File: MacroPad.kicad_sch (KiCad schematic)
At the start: 41 parts, among them J1 USB_C_Receptacle, SW1 SW_Push, U1 ATmega32U4-A, Y1 16MHz

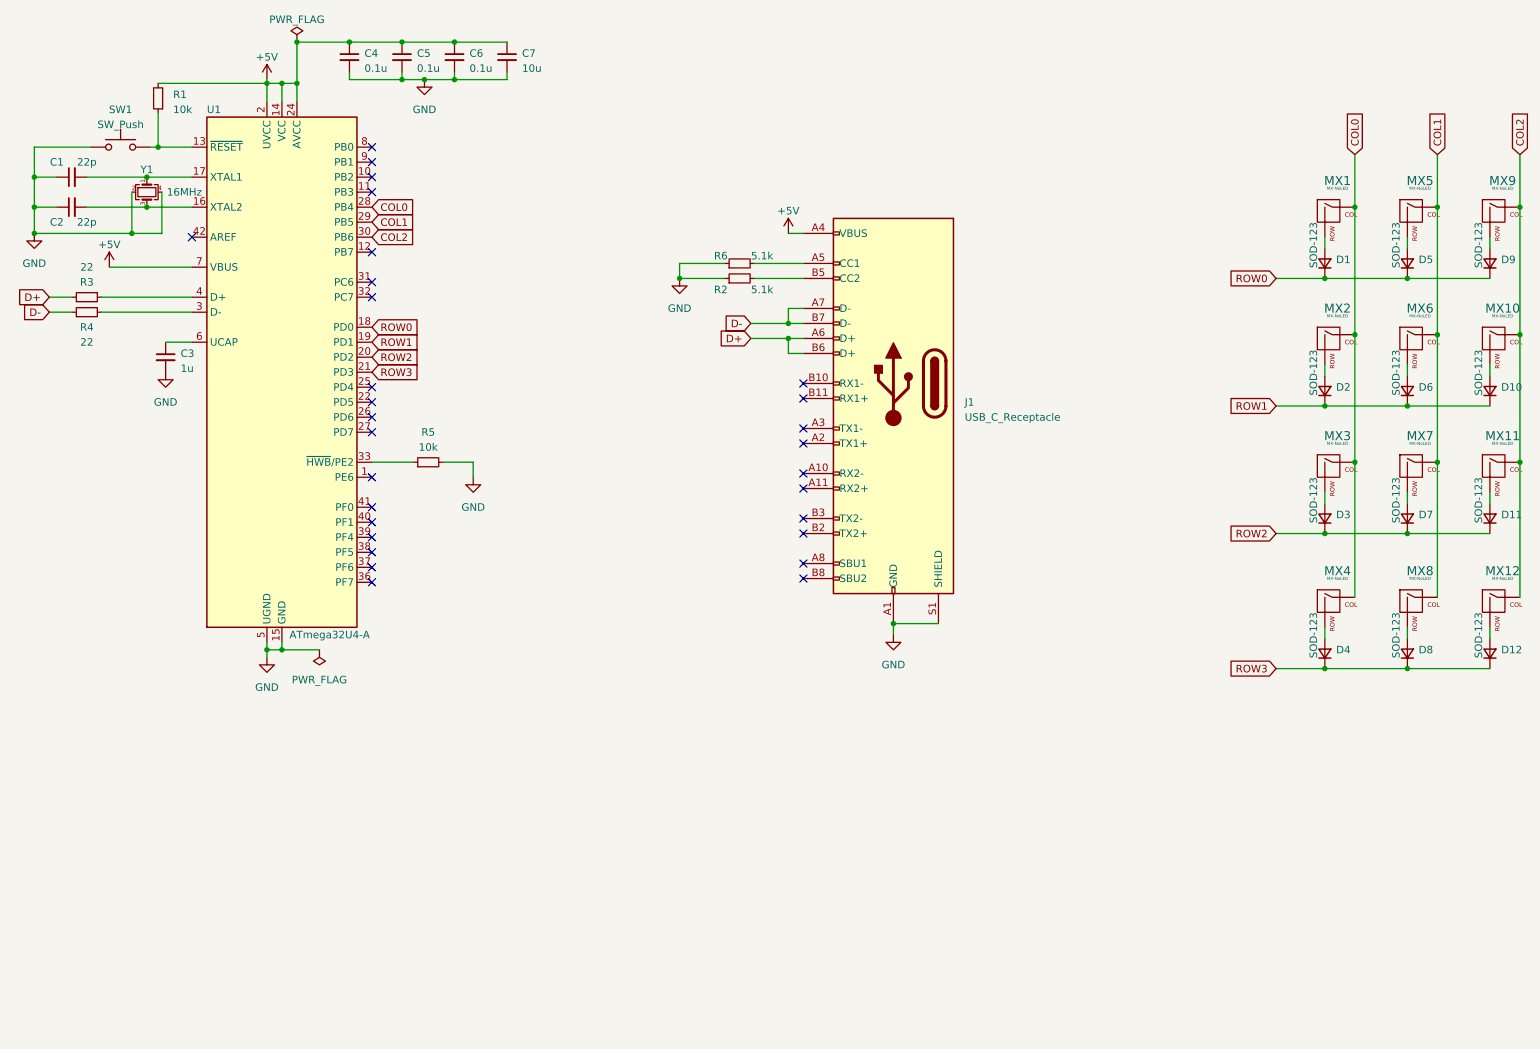
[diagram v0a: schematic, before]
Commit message: reworked schematic, added footprint library for USB-C, improved component placement
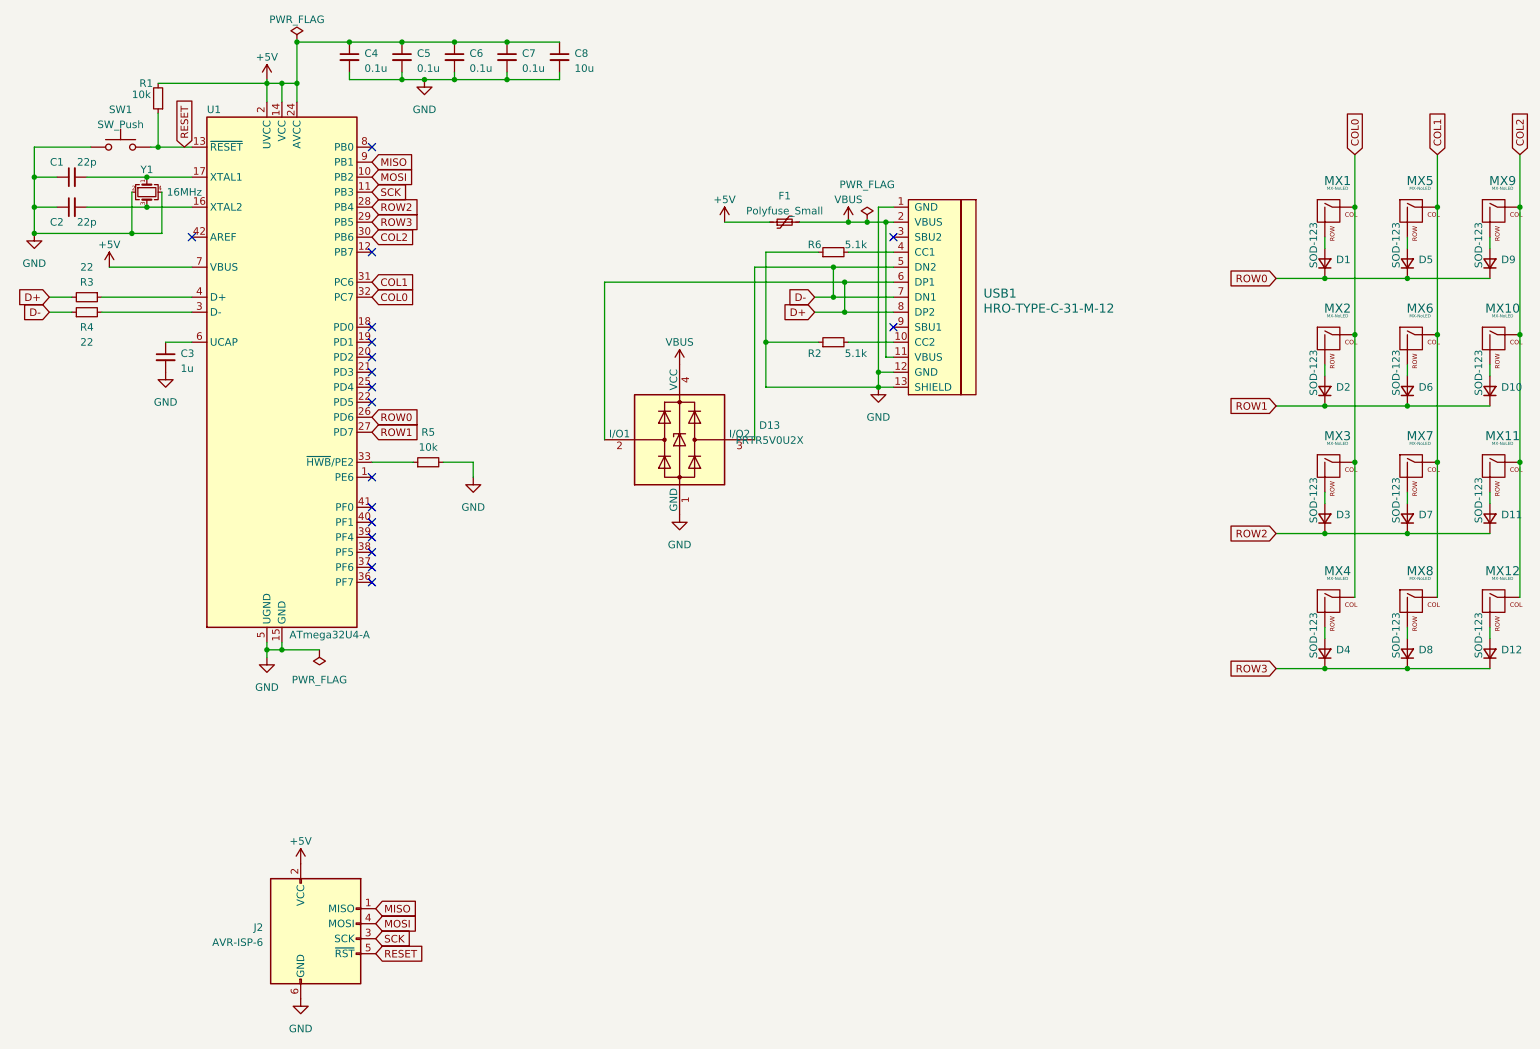
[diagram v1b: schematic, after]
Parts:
- removed J1: USB_C_Receptacle, Connector_USB:USB_C_Receptacle_GCT_USB4105-xx-A_16P_TopMnt_Horizontal, symbol Connector:USB_C_Receptacle
- added C8: 10u, Capacitor_SMD:C_0805_2012Metric, symbol Device:C_Small
- added D13: PRTR5V0U2X, Package_TO_SOT_SMD:SOT-143, symbol Power_Protection:PRTR5V0U2X
- added F1: Polyfuse_Small, Fuse:Fuse_1206_3216Metric_Pad1.42x1.75mm_HandSolder, symbol Device:Polyfuse_Small
- added J2: AVR-ISP-6, random-keyboard-parts:Reset_Pretty-Mask, symbol Connector:AVR-ISP-6
- added USB1: HRO-TYPE-C-31-M-12, Type-C:HRO-TYPE-C-31-M-12-HandSoldering, symbol Type-C:HRO-TYPE-C-31-M-12
- C7: value 10u -> 0.1u
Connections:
- net +5V: now also C8.1, F1.1, J2.2 (VCC)
- net COL0: now also U1.32 (PC7); no longer U1.28 (PB4)
- net COL1: now also U1.31 (PC6); no longer U1.29 (PB5)
- net D+: now also D13.2 (I/O1), USB1.6 (DP1), USB1.8 (DP2)
- net D-: now also D13.3 (I/O2), USB1.5 (DN2), USB1.7 (DN1)
- net GND: now also C8.2, D13.1 (GND), J2.6 (GND), USB1.1 (GND), USB1.12 (GND), USB1.13 (SHIELD)
- net ROW0: now also U1.26 (PD6); no longer U1.18 (PD0)
- net ROW1: now also U1.27 (PD7); no longer U1.19 (PD1)
- net ROW2: now also U1.28 (PB4); no longer U1.20 (PD2)
- net ROW3: now also U1.29 (PB5); no longer U1.21 (PD3)
- net at R6.2: now also USB1.4 (CC1)
- net RESET: now reaches R1.1, SW1.2, U1.13 (~{RESET})
- net RESET: now also J2.5 (~{RST})
- net MOSI: now reaches U1.10 (PB2)
- net MOSI: now also J2.4 (MOSI)
- net SCK: now reaches U1.11 (PB3)
- net SCK: now also J2.3 (SCK)
- net MISO: now reaches U1.9 (PB1)
- net MISO: now also J2.1 (MISO)
- net at R2.2: now also USB1.10 (CC2)
- new net VBUS: D13.4 (VCC), F1.2, USB1.11 (VBUS), USB1.2 (VBUS)
- no-connect marks 29 -> 18
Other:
- moved on the sheet: R2, R6

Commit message: finished placement, routing and overall layout
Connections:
- net COL0: now also U1.1 (PE6); no longer U1.32 (PC7)
- net COL1: now also U1.41 (PF0); no longer U1.31 (PC6)
- net COL2: now also U1.40 (PF1); no longer U1.30 (PB6)
- net ROW0: now also U1.36 (PF7); no longer U1.26 (PD6)
- net ROW1: now also U1.37 (PF6); no longer U1.27 (PD7)
- net ROW2: now also U1.38 (PF5); no longer U1.28 (PB4)
- net ROW3: now also U1.39 (PF4); no longer U1.29 (PB5)
- net DP: now reaches R3.1, U1.4 (D+)
- net DN: now reaches R4.2, U1.3 (D-)
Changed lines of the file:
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@@
   (junction (at 38.1 33.02) (diameter 0) (color 0 0 0 0)
   )
-  (no_connect (at 74.295 106.68))
+  (no_connect (at 74.295 78.74))
   (no_connect (at 162.56 63.5))
-  (no_connect (at 74.295 101.6))
   (no_connect (at 74.295 66.04))
   (no_connect (at 74.295 73.66))
   (no_connect (at 74.295 33.02))
   (no_connect (at 74.295 68.58))
-  (no_connect (at 74.295 96.52))
+  (no_connect (at 74.295 81.28))
+  (no_connect (at 74.295 45.72))
   (no_connect (at 43.815 48.26))
   (no_connect (at 74.295 63.5))
-  (no_connect (at 74.295 88.9))
   (no_connect (at 74.295 50.8))
-  (no_connect (at 74.295 93.98))
   (no_connect (at 162.56 48.26))
-  (no_connect (at 74.295 104.14))
+  (no_connect (at 74.295 43.18))
+  (no_connect (at 74.295 55.88))
+  (no_connect (at 74.295 48.26))
+  (no_connect (at 74.295 58.42))
   (no_connect (at 74.295 76.2))
   (no_connect (at 74.295 71.12))
-  (no_connect (at 74.295 99.06))
   (wire (pts (xy 19.685 58.42) (xy 23.495 58.42))
     (stroke (width 0) (type default))
@@
     )
   )
-  (global_label "ROW3" (shape input) (at 74.295 45.72 0) (fields_autoplaced)
-    (effects (font (size 1.27 1.27)) (justify left))
-    (property "Intersheetrefs" "${INTERSHEET_REFS}" (at 82.4622 45.72 0)
+  (global_label "ROW3" (shape input) (at 74.295 99.06 0) (fields_autoplaced)
+    (effects (font (size 1.27 1.27)) (justify left))
+    (property "Intersheetrefs" "${INTERSHEET_REFS}" (at 82.4622 99.06 0)
       (effects (font (size 1.27 1.27)) (justify left) hide)
     )
@@
     )
   )
-  (global_label "ROW1" (shape input) (at 74.295 81.28 0) (fields_autoplaced)
-    (effects (font (size 1.27 1.27)) (justify left))
-    (property "Intersheetrefs" "${INTERSHEET_REFS}" (at 82.4622 81.28 0)
+  (global_label "ROW1" (shape input) (at 74.295 104.14 0) (fields_autoplaced)
+    (effects (font (size 1.27 1.27)) (justify left))
+    (property "Intersheetrefs" "${INTERSHEET_REFS}" (at 82.4622 104.14 0)
       (effects (font (size 1.27 1.27)) (justify left) hide)
     )
@@
     )
   )
+  (global_label "DP" (shape input) (at 33.655 58.42 90) (fields_autoplaced)
+    (effects (font (size 1.27 1.27)) (justify left))
+    (property "Intersheetrefs" "${INTERSHEET_REFS}" (at 33.655 52.9742 90)
+      (effects (font (size 1.27 1.27)) (justify left) hide)
+    )
+  )
   (global_label "D+" (shape input) (at 19.685 58.42 180) (fields_autoplaced)
     (effects (font (size 1.27 1.27)) (justify right))
@@
     )
   )
-  (global_label "COL2" (shape input) (at 74.295 48.26 0) (fields_autoplaced)
-    (effects (font (size 1.27 1.27)) (justify left))
-    (property "Intersheetrefs" "${INTERSHEET_REFS}" (at 82.0389 48.26 0)
+  (global_label "COL2" (shape input) (at 74.295 96.52 0) (fields_autoplaced)
+    (effects (font (size 1.27 1.27)) (justify left))
+    (property "Intersheetrefs" "${INTERSHEET_REFS}" (at 82.0389 96.52 0)
       (effects (font (size 1.27 1.27)) (justify left) hide)
     )
@@
     )
   )
-  (global_label "COL1" (shape input) (at 74.295 55.88 0) (fields_autoplaced)
-    (effects (font (size 1.27 1.27)) (justify left))
-    (property "Intersheetrefs" "${INTERSHEET_REFS}" (at 82.0389 55.88 0)
+  (global_label "COL1" (shape input) (at 74.295 93.98 0) (fields_autoplaced)
+    (effects (font (size 1.27 1.27)) (justify left))
+    (property "Intersheetrefs" "${INTERSHEET_REFS}" (at 82.0389 93.98 0)
       (effects (font (size 1.27 1.27)) (justify left) hide)
     )
@@
     )
   )
-  (global_label "COL0" (shape input) (at 74.295 58.42 0) (fields_autoplaced)
-    (effects (font (size 1.27 1.27)) (justify left))
-    (property "Intersheetrefs" "${INTERSHEET_REFS}" (at 82.0389 58.42 0)
+  (global_label "COL0" (shape input) (at 74.295 88.9 0) (fields_autoplaced)
+    (effects (font (size 1.27 1.27)) (justify left))
+    (property "Intersheetrefs" "${INTERSHEET_REFS}" (at 82.0389 88.9 0)
       (effects (font (size 1.27 1.27)) (justify left) hide)
     )
@@
     )
   )
-  (global_label "ROW2" (shape input) (at 74.295 43.18 0) (fields_autoplaced)
-    (effects (font (size 1.27 1.27)) (justify left))
-    (property "Intersheetrefs" "${INTERSHEET_REFS}" (at 82.4622 43.18 0)
+  (global_label "ROW2" (shape input) (at 74.295 101.6 0) (fields_autoplaced)
+    (effects (font (size 1.27 1.27)) (justify left))
+    (property "Intersheetrefs" "${INTERSHEET_REFS}" (at 82.4622 101.6 0)
       (effects (font (size 1.27 1.27)) (justify left) hide)
     )
@@
     )
   )
+  (global_label "DN" (shape input) (at 33.655 60.96 270) (fields_autoplaced)
+    (effects (font (size 1.27 1.27)) (justify right))
+    (property "Intersheetrefs" "${INTERSHEET_REFS}" (at 33.655 66.4663 90)
+      (effects (font (size 1.27 1.27)) (justify right) hide)
+    )
+  )
   (global_label "ROW3" (shape input) (at 227.33 121.285 180) (fields_autoplaced)
     (effects (font (size 1.27 1.27)) (justify right))
@@
     )
   )
-  (global_label "ROW0" (shape input) (at 74.295 78.74 0) (fields_autoplaced)
-    (effects (font (size 1.27 1.27)) (justify left))
-    (property "Intersheetrefs" "${INTERSHEET_REFS}" (at 82.4622 78.74 0)
-      (effects (font (size 1.27 1.27)) (justify left) hide)
-    )
+  (global_label "ROW0" (shape input) (at 74.295 106.68 0) (fields_autoplaced)
+    (effects (font (size 1.27 1.27)) (justify left))
+    (property "Intersheetrefs" "${INTERSHEET_REFS}" (at 82.4622 106.68 0)
+      (effects (font (size 1.27 1.27)) (justify left) hide)
+    )
